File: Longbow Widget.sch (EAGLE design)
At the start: 31 parts, among them J0 CONN_6SCREW_2.54, J1 CONN_6SCREW_2.54, J2 87832-14, Q2 DMG3404, Q6 FDN360P, U1 TPS7A0533DBV

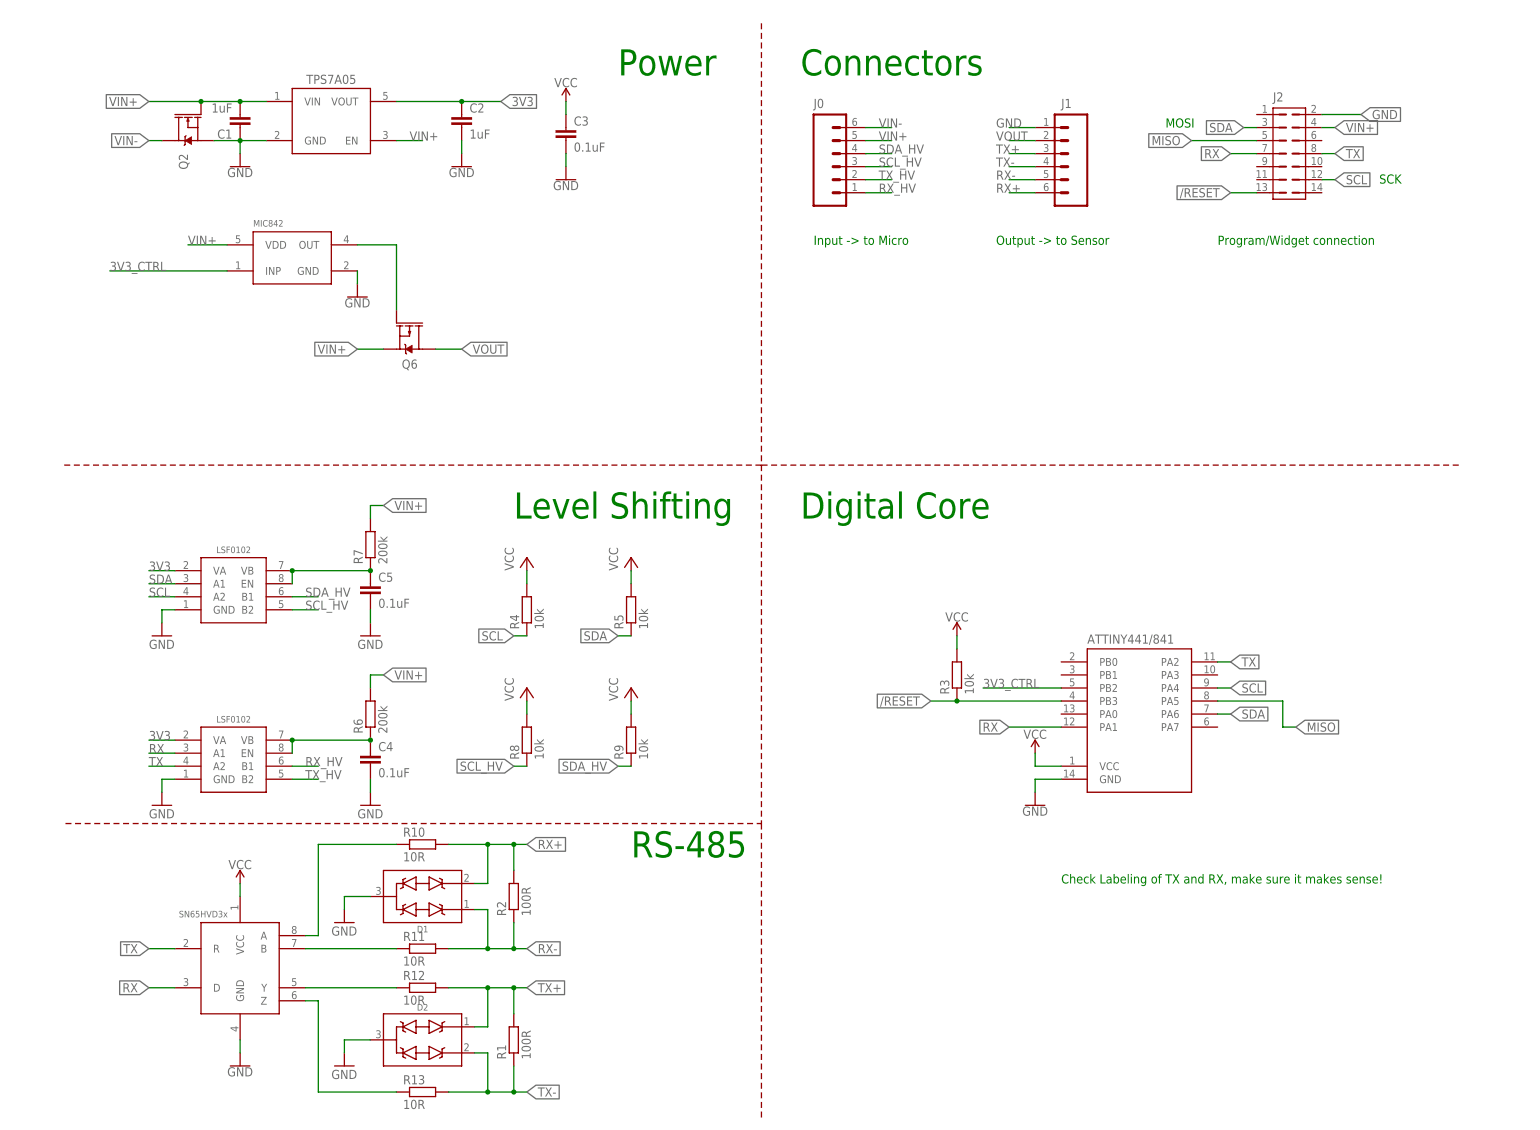
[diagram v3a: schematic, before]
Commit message: Final designs for Longbow Widget v0.1 and Universal Breakout Pogo board
Added final design (minor silk screen additions) of the Longbow widget, also designed a modified Universal breakout which has support for pogo pins. Generated final gerbers for both as well
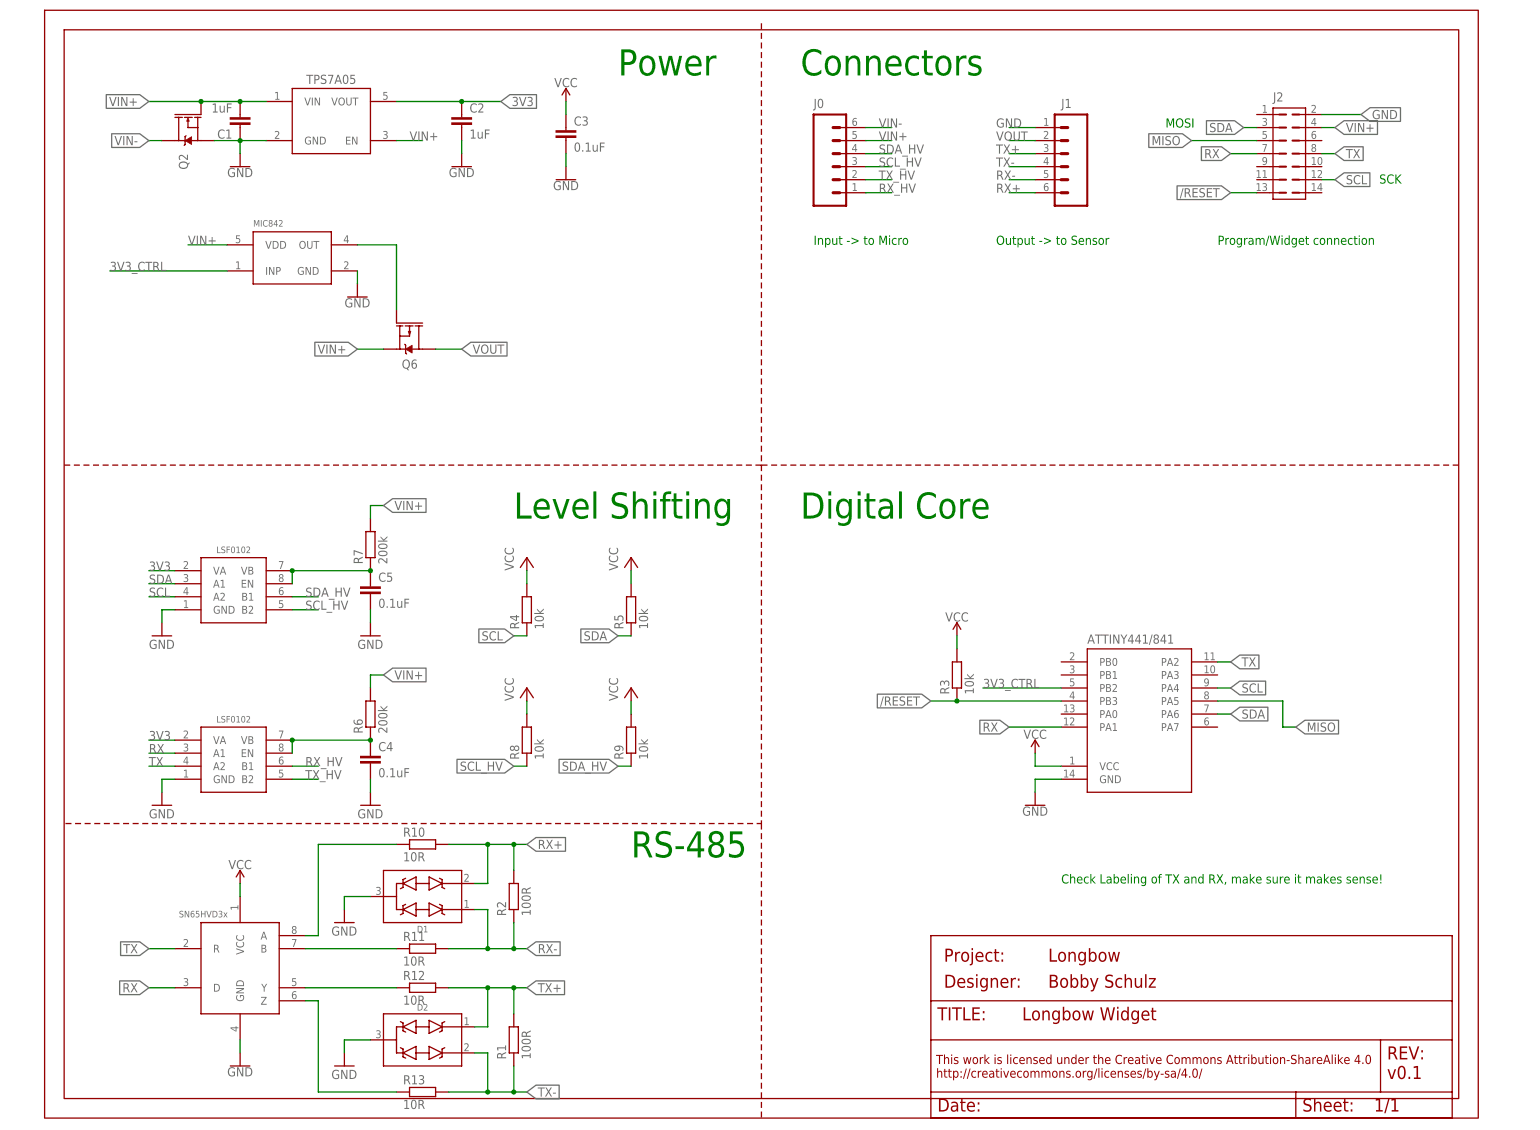
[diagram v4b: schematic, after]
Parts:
- added FRAME1: (no value), bschulz:FRAME_A_L
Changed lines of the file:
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@@
 <setting verticaltext="up"/>
 </settings>
-<grid distance="0.1" unitdist="inch" unit="mm" style="lines" multiple="1" display="no" altdistance="0.01" altunitdist="inch" altunit="mm"/>
+<grid distance="0.1" unitdist="inch" unit="inch" style="lines" multiple="1" display="no" altdistance="0.01" altunitdist="inch" altunit="inch"/>
 <layers>
-<layer number="1" name="Top" color="4" fill="1" visible="yes" active="no"/>
-<layer number="2" name="Route2" color="1" fill="3" visible="yes" active="no"/>
-<layer number="3" name="Route3" color="4" fill="3" visible="yes" active="no"/>
-<layer number="4" name="Route4" color="1" fill="4" visible="yes" active="no"/>
-<layer number="5" name="Route5" color="4" fill="4" visible="yes" active="no"/>
-<layer number="6" name="Route6" color="1" fill="8" visible="yes" active="no"/>
-<layer number="7" name="Route7" color="4" fill="8" visible="yes" active="no"/>
-<layer number="8" name="Route8" color="1" fill="2" visible="yes" active="no"/>
-<layer number="9" name="Route9" color="4" fill="2" visible="yes" active="no"/>
-<layer number="10" name="Route10" color="1" fill="7" visible="yes" active="no"/>
-<layer number="11" name="Route11" color="4" fill="7" visible="yes" active="no"/>
-<layer number="12" name="Route12" color="1" fill="5" visible="yes" active="no"/>
-<layer number="13" name="Route13" color="4" fill="5" visible="yes" active="no"/>
-<layer number="14" name="Route14" color="1" fill="6" visible="yes" active="no"/>
-<layer number="15" name="Route15" color="4" fill="6" visible="yes" active="no"/>
-<layer number="16" name="Bottom" color="1" fill="1" visible="yes" active="no"/>
-<layer number="17" name="Pads" color="2" fill="1" visible="yes" active="no"/>
-<layer number="18" name="Vias" color="2" fill="1" visible="yes" active="no"/>
-<layer number="19" name="Unrouted" color="6" fill="1" visible="yes" active="no"/>
-<layer number="20" name="Dimension" color="24" fill="1" visible="yes" active="no"/>
-<layer number="21" name="tPlace" color="7" fill="1" visible="yes" active="no"/>
-<layer number="22" name="bPlace" color="7" fill="1" visible="yes" active="no"/>
-<layer number="23" name="tOrigins" color="15" fill="1" visible="yes" active="no"/>
-<layer number="24" name="bOrigins" color="15" fill="1" visible="yes" active="no"/>
-<layer number="25" name="tNames" color="7" fill="1" visible="yes" active="no"/>
-<layer number="26" name="bNames" color="7" fill="1" visible="yes" active="no"/>
-<layer number="27" name="tValues" color="7" fill="1" visible="yes" active="no"/>
-<layer number="28" name="bValues" color="7" fill="1" visible="yes" active="no"/>
+<layer number="1" name="Top" color="4" fill="1" visible="no" active="no"/>
+<layer number="2" name="Route2" color="1" fill="3" visible="no" active="no"/>
+<layer number="3" name="Route3" color="4" fill="3" visible="no" active="no"/>
+<layer number="4" name="Route4" color="1" fill="4" visible="no" active="no"/>
+<layer number="5" name="Route5" color="4" fill="4" visible="no" active="no"/>
+<layer number="6" name="Route6" color="1" fill="8" visible="no" active="no"/>
+<layer number="7" name="Route7" color="4" fill="8" visible="no" active="no"/>
+<layer number="8" name="Route8" color="1" fill="2" visible="no" active="no"/>
+<layer number="9" name="Route9" color="4" fill="2" visible="no" active="no"/>
+<layer number="10" name="Route10" color="1" fill="7" visible="no" active="no"/>
+<layer number="11" name="Route11" color="4" fill="7" visible="no" active="no"/>
+<layer number="12" name="Route12" color="1" fill="5" visible="no" active="no"/>
+<layer number="13" name="Route13" color="4" fill="5" visible="no" active="no"/>
+<layer number="14" name="Route14" color="1" fill="6" visible="no" active="no"/>
+<layer number="15" name="Route15" color="4" fill="6" visible="no" active="no"/>
+<layer number="16" name="Bottom" color="1" fill="1" visible="no" active="no"/>
+<layer number="17" name="Pads" color="2" fill="1" visible="no" active="no"/>
+<layer number="18" name="Vias" color="2" fill="1" visible="no" active="no"/>
+<layer number="19" name="Unrouted" color="6" fill="1" visible="no" active="no"/>
+<layer number="20" name="Dimension" color="24" fill="1" visible="no" active="no"/>
+<layer number="21" name="tPlace" color="7" fill="1" visible="no" active="no"/>
+<layer number="22" name="bPlace" color="7" fill="1" visible="no" active="no"/>
+<layer number="23" name="tOrigins" color="15" fill="1" visible="no" active="no"/>
+<layer number="24" name="bOrigins" color="15" fill="1" visible="no" active="no"/>
+<layer number="25" name="tNames" color="7" fill="1" visible="no" active="no"/>
+<layer number="26" name="bNames" color="7" fill="1" visible="no" active="no"/>
+<layer number="27" name="tValues" color="7" fill="1" visible="no" active="no"/>
+<layer number="28" name="bValues" color="7" fill="1" visible="no" active="no"/>
 <layer number="29" name="tStop" color="7" fill="3" visible="no" active="no"/>
 <layer number="30" name="bStop" color="7" fill="6" visible="no" active="no"/>
@@
 <layer number="35" name="tGlue" color="7" fill="4" visible="no" active="no"/>
 <layer number="36" name="bGlue" color="7" fill="5" visible="no" active="no"/>
-<layer number="37" name="tTest" color="7" fill="1" visible="yes" active="no"/>
-<layer number="38" name="bTest" color="7" fill="1" visible="yes" active="no"/>
+<layer number="37" name="tTest" color="7" fill="1" visible="no" active="no"/>
+<layer number="38" name="bTest" color="7" fill="1" visible="no" active="no"/>
 <layer number="39" name="tKeepout" color="4" fill="11" visible="no" active="no"/>
 <layer number="40" name="bKeepout" color="1" fill="11" visible="no" active="no"/>
@@
 <layer number="44" name="Drills" color="7" fill="1" visible="no" active="no"/>
 <layer number="45" name="Holes" color="7" fill="1" visible="no" active="no"/>
-<layer number="46" name="Milling" color="3" fill="1" visible="yes" active="no"/>
-<layer number="47" name="Measures" color="7" fill="1" visible="yes" active="no"/>
-<layer number="48" name="Document" color="7" fill="1" visible="yes" active="no"/>
-<layer number="49" name="Reference" color="7" fill="1" visible="yes" active="no"/>
-<layer number="50" name="dxf" color="7" fill="1" visible="yes" active="no"/>
-<layer number="51" name="tDocu" color="7" fill="1" visible="yes" active="no"/>
-<layer number="52" name="bDocu" color="7" fill="1" visible="yes" active="no"/>
-<layer number="53" name="tGND_GNDA" color="7" fill="1" visible="yes" active="no"/>
-<layer number="54" name="bGND_GNDA" color="7" fill="1" visible="yes" active="no"/>
-<layer number="56" name="wert" color="7" fill="1" visible="yes" active="no"/>
-<layer number="57" name="tCAD" color="7" fill="1" visible="yes" active="no"/>
-<layer number="59" name="tCarbon" color="7" fill="1" visible="yes" active="no"/>
-<layer number="60" name="bCarbon" color="7" fill="1" visible="yes" active="no"/>
+<layer number="46" name="Milling" color="3" fill="1" visible="no" active="no"/>
+<layer number="47" name="Measures" color="7" fill="1" visible="no" active="no"/>
+<layer number="48" name="Document" color="7" fill="1" visible="no" active="no"/>
+<layer number="49" name="Reference" color="7" fill="1" visible="no" active="no"/>
+<layer number="50" name="dxf" color="7" fill="1" visible="no" active="no"/>
+<layer number="51" name="tDocu" color="7" fill="1" visible="no" active="no"/>
+<layer number="52" name="bDocu" color="7" fill="1" visible="no" active="no"/>
+<layer number="53" name="tGND_GNDA" color="7" fill="1" visible="no" active="no"/>
+<layer number="54" name="bGND_GNDA" color="7" fill="1" visible="no" active="no"/>
+<layer number="56" name="wert" color="7" fill="1" visible="no" active="no"/>
+<layer number="57" name="tCAD" color="7" fill="1" visible="no" active="no"/>
+<layer number="59" name="tCarbon" color="7" fill="1" visible="no" active="no"/>
+<layer number="60" name="bCarbon" color="7" fill="1" visible="no" active="no"/>
 <layer number="88" name="SimResults" color="9" fill="1" visible="yes" active="yes"/>
 <layer number="89" name="SimProbes" color="9" fill="1" visible="yes" active="yes"/>
@@
 <attribute name="DESIGNER" value="Bobby Schulz"/>
 <attribute name="PROJECT" value="Longbow"/>
-<attribute name="REV" value="0.1"/>
+<attribute name="REV" value="v0.1"/>
 </part>
 <part name="C4" library="bschulz_passives" deviceset="C-EU" device="C0402" technology="0.1UF" value="0.1uF"/>

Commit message: Fixed part numbers on Longbow Widget, generated new BOMs
Parts list is updated and fully auto generating
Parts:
- J2: value 87832-14 -> 87832-14MALE; device bschulz:87832-14 -> bschulz:87832-14MALE
- R1, R2: device bschulz_passives:R-EU_R0402 -> bschulz_passives:R-EU_100R0402
- R10, R11, R12, R13: DIGIKEY (none) -> 541-10.0SCT-ND; MF (none) -> Vishay; MPN (none) -> CRCW060310R0FKEAHP; VALUE_PART (none) -> 10
- R6, R7: device bschulz_passives:R-EU_R0402 -> bschulz_passives:R-EU_200KR0402
